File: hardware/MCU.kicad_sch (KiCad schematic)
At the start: 1 part

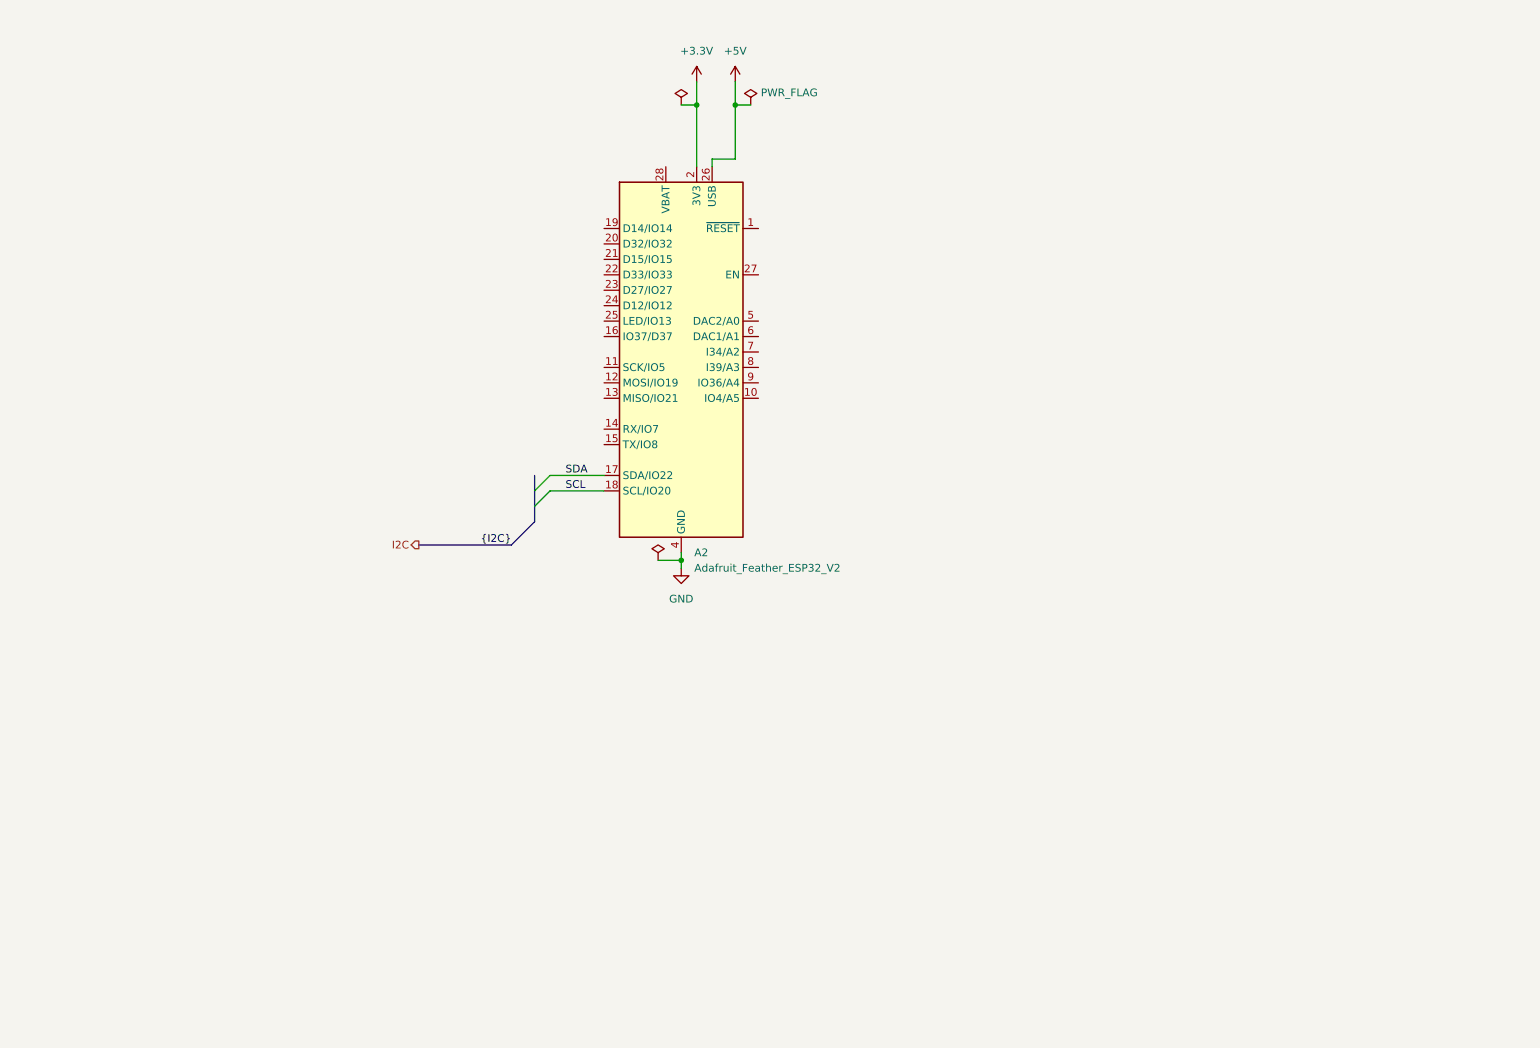
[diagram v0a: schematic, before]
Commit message: feat: Added MCP23017 SOIC GPIO Expander
Finished off the design of all of the non-GPIO pins of the expander
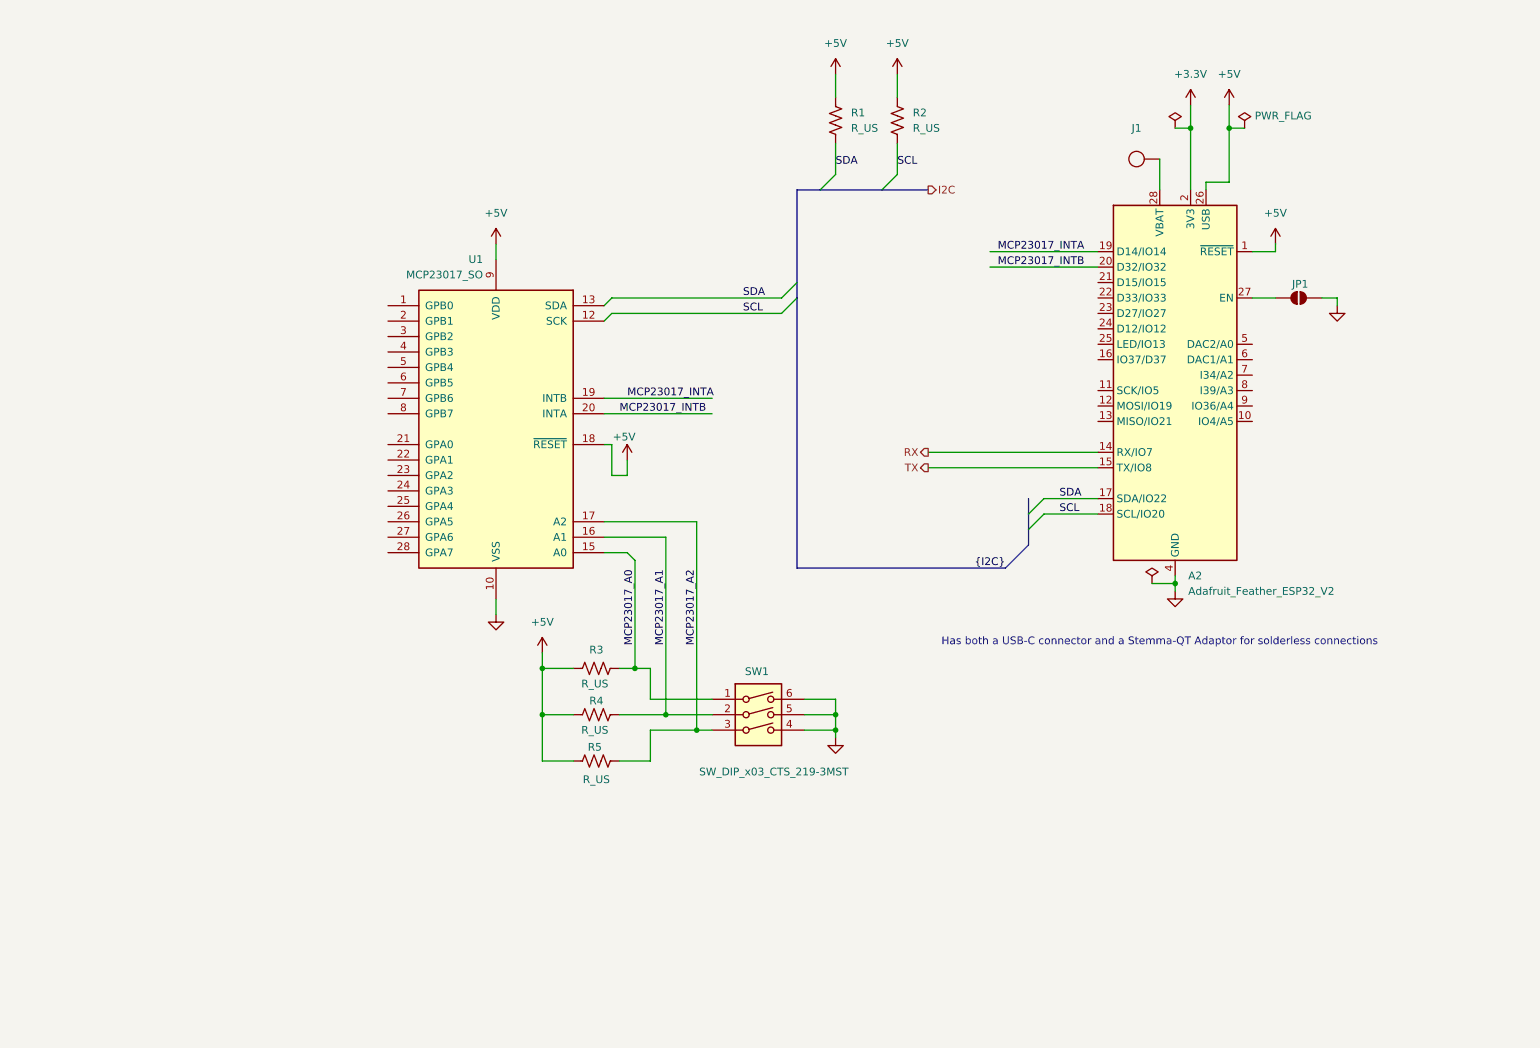
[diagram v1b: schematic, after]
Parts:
- added J1: ~, 4ms_Connector:CAPSENSE_PAD, symbol 4ms_Connector:CAPSENSE_PAD
- added JP1: SolderJumper_2_Open, Jumper:SolderJumper-2_P1.3mm_Open_Pad1.0x1.5mm, symbol Jumper:SolderJumper_2_Open
- added R1, R2, R3, R4, R5: R_US, symbol Device:R_US
- added SW1: SW_DIP_x03_CTS_219-3MST, 4ms_Switch:SW_DIP_SPSTx03_CTS_219-3MSTR, symbol 4ms_Switch:SW_DIP_x03_CTS_219-3MST
- added U1: MCP23017_SO, Package_SO:SOIC-28W_7.5x17.9mm_P1.27mm, symbol Interface_Expansion:MCP23017_SO
- A2: now left out of the parts list
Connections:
- net +5V: now also A2.1 (~{RESET}), R1.1, R2.1, R3.1, R4.1, R5.1, U1.18 (~{RESET}), U1.9 (VDD)
- net GND: now also JP1.2 (B), SW1.4, SW1.5, SW1.6, U1.10 (VSS)
- net SCL: now also R2.2, U1.12 (SCK)
- net SDA: now also R1.2, U1.13 (SDA)
- net RX: now reaches A2.14 (RX/IO7)
- net TX: now reaches A2.15 (TX/IO8)
- net MCP23017_INTA: now reaches A2.19 (D14/IO14)
- net MCP23017_INTA: now also U1.19 (INTB)
- net MCP23017_INTB: now reaches A2.20 (D32/IO32)
- net MCP23017_INTB: now also U1.20 (INTA)
- net at A2.27 (EN): now also JP1.1 (A)
- net at A2.28 (VBAT): now also J1.1 (CS)
- new net MCP23017_A0: R3.2, SW1.1, U1.15 (A0)
- new net MCP23017_A1: R4.2, SW1.2, U1.16 (A1)
- new net MCP23017_A2: R5.2, SW1.3, U1.17 (A2)
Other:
- note added: "Has both a USB-C connector and a Stemma-QT Adaptor for solderless connections"
- moved on the sheet: A2

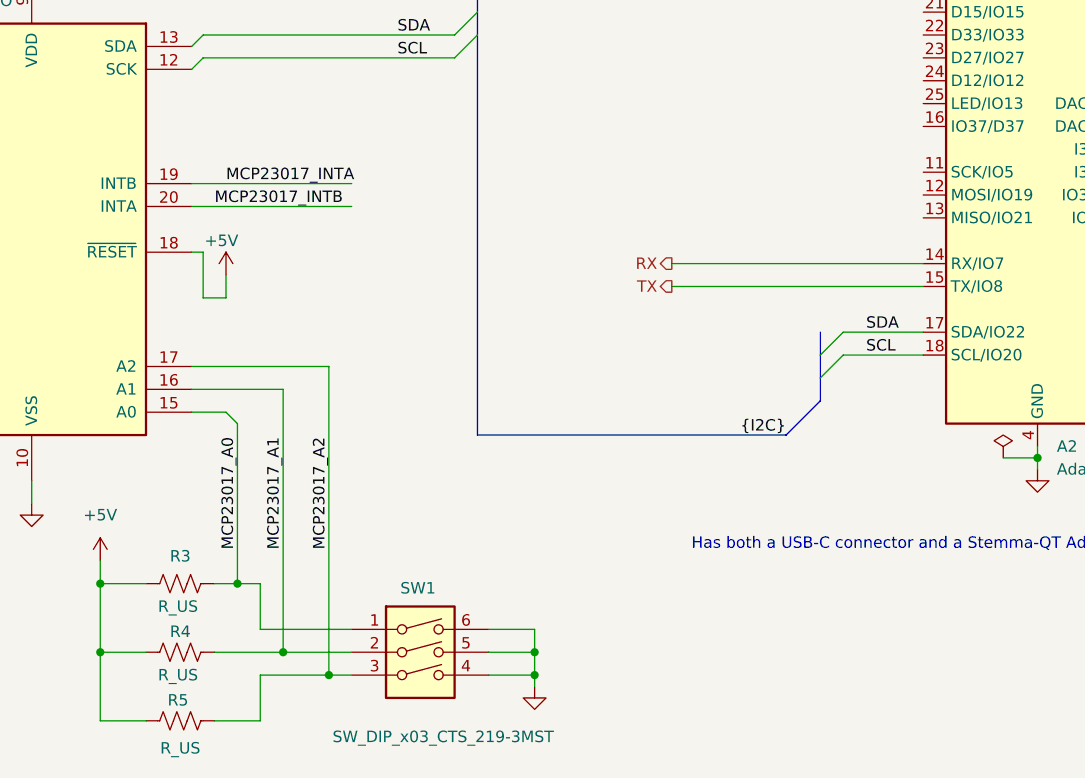
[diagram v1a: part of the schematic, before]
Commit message: feat: Created Button I2C Interfaces
For now, all we are using is generic 1x5 Connectors following the DFR Robot's RGB Button pinout https://wiki.dfrobot.com/SKU_DFR0991_Gravity_I2C_RGB_LED_Button_Module#target_9
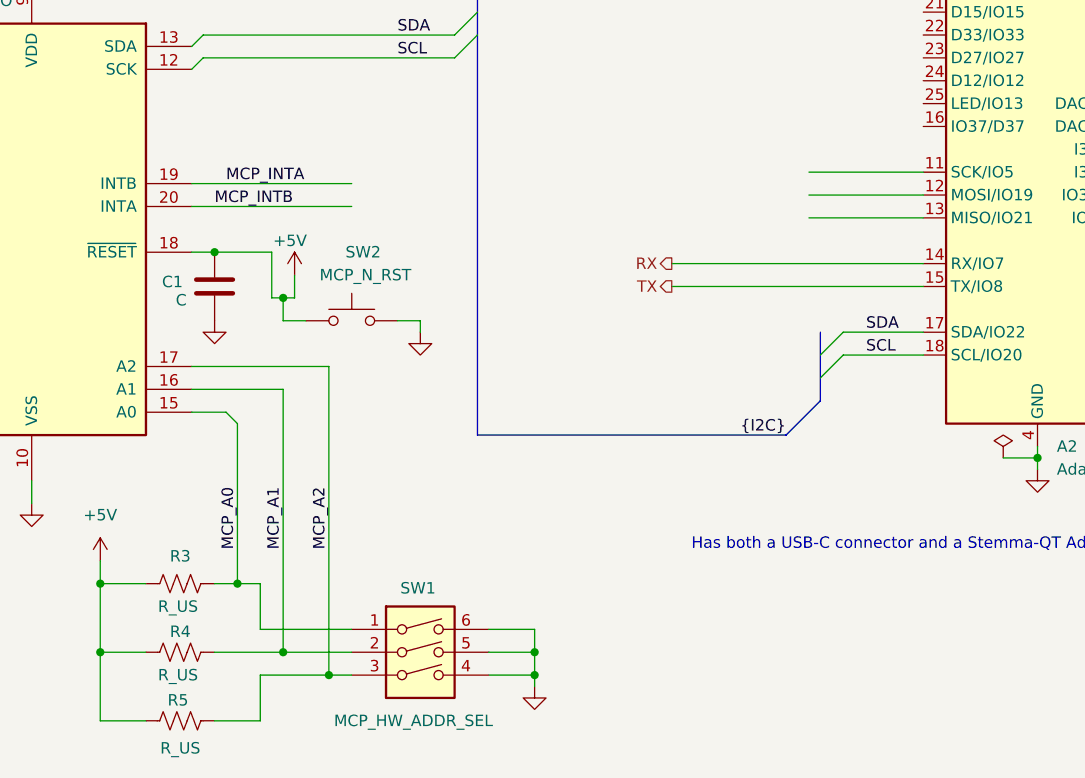
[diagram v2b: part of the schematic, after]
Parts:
- added C1: C, symbol Device:C
- added SW2: MCP_N_RST, symbol Switch:SW_Push
- SW1: value SW_DIP_x03_CTS_219-3MST -> MCP_HW_ADDR_SEL
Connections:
- net +5V: now also C1.1, SW2.1
- net GND: now also C1.2, SW2.2
- net MCP23017_INTA: no longer U1.19 (INTB)
- net MCP23017_INTB: no longer U1.20 (INTA)
- net MCP23017_A0 renamed MCP_A0
- net MCP23017_A1 renamed MCP_A1
- net MCP23017_A2 renamed MCP_A2
- new net MCP_INTA: U1.19 (INTB)
- new net MCP_INTB: U1.20 (INTA)

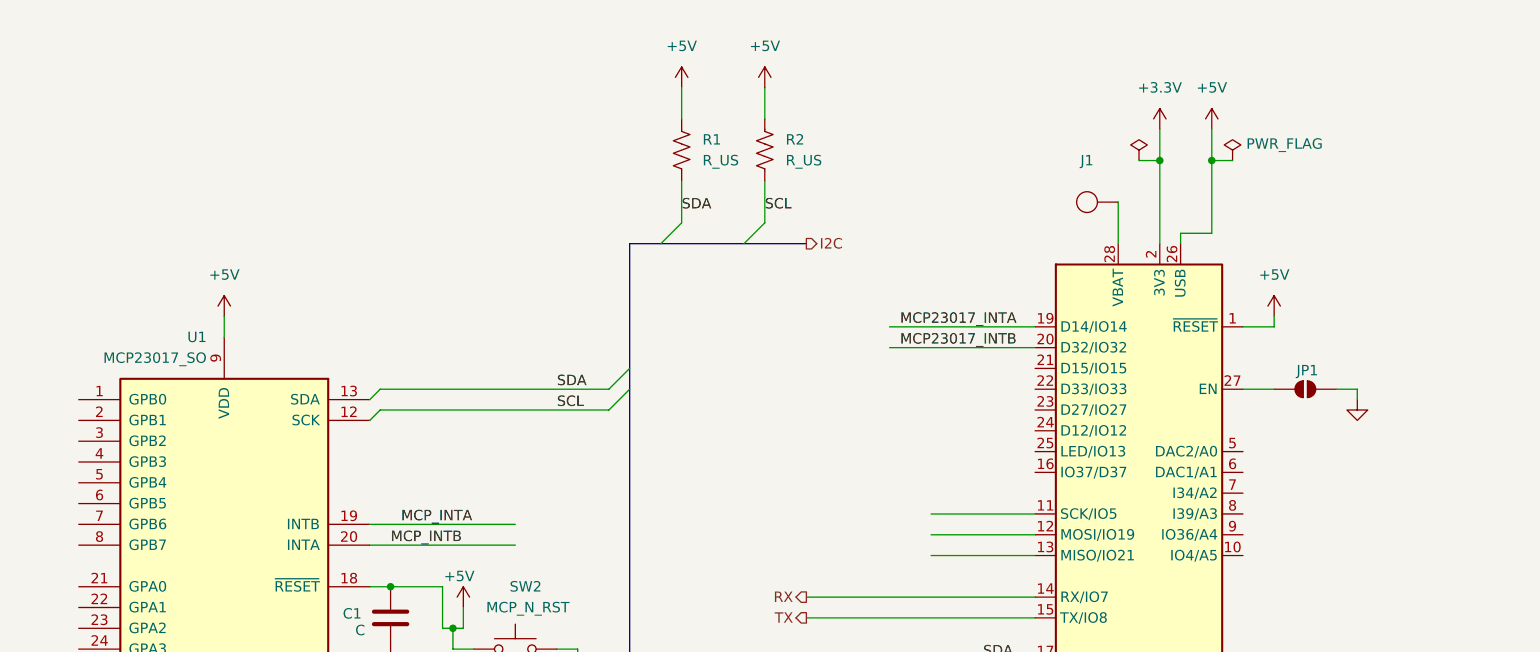
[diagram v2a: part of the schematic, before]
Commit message: feat: Added Volume and Inf Scroll Encoders
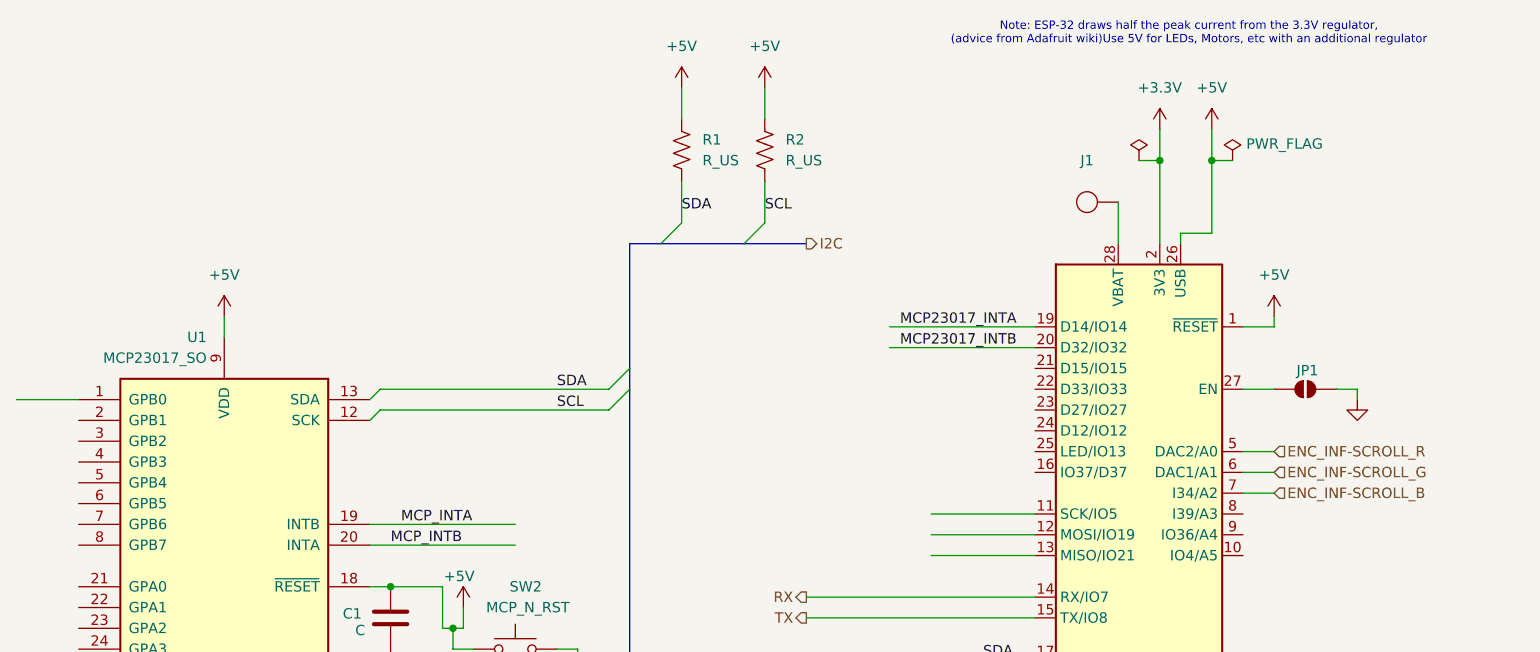
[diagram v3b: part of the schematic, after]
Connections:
- net ENC_INF-SCROLL_R: now reaches A2.5 (DAC2/A0)
- net ENC_INF-SCROLL_G: now reaches A2.6 (DAC1/A1)
- net ENC_INF-SCROLL_B: now reaches A2.7 (I34/A2)
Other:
- note added: "Note: ESP-32 draws half the peak current from the 3.3V regulator, (advice from Adafruit wiki)Use 5V for LEDs, Motors, etc with an additional regulator"
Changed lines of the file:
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@@
+		)
+	)
+	(text "Note: ESP-32 draws half the peak current from the 3.3V regulator,\n(advice from Adafruit wiki)Use 5V for LEDs, Motors, etc with an additional regulator"
+		(exclude_from_sim no)
+		(at 211.836 17.526 0)
+		(effects
+			(font
+				(size 1.016 1.016)
+			)
+			(href "https://learn.adafruit.com/adafruit-esp32-feather-v2/power-management-2")
 		)
 	)
@@
 	(wire
 		(pts
+			(xy 218.44 71.12) (xy 222.25 71.12)
+		)
+		(stroke
+			(width 0)
+			(type default)
+		)
+	)
+	(wire
+		(pts
+			(xy 218.44 68.58) (xy 222.25 68.58)
+		)
+		(stroke
+			(width 0)
+			(type default)
+		)
+	)
+	(wire
+		(pts
 			(xy 232.41 60.96) (xy 232.41 62.23)
 		)
@@
 	(wire
 		(pts
+			(xy 68.58 62.23) (xy 76.2 62.23)
+		)
+		(stroke
+			(width 0)
+			(type default)
+		)
+	)
+	(wire
+		(pts
 			(xy 93.98 110.49) (xy 93.98 113.03)
 		)
@@
 		(pts
 			(xy 119.38 127) (xy 129.54 127)
+		)
+		(stroke
+			(width 0)
+			(type default)
+		)
+	)
+	(wire
+		(pts
+			(xy 218.44 73.66) (xy 222.25 73.66)
 		)
 		(stroke
@@
 			)
 			(justify left bottom)
+		)
+	)
+	(hierarchical_label "ENC_INF-SCROLL_B"
+		(shape input)
+		(at 222.25 73.66 0)
+		(effects
+			(font
+				(size 1.27 1.27)
+			)
+			(justify left)
+		)
+	)
+	(hierarchical_label "ENC_INF-SCROLL_G"
+		(shape input)
+		(at 222.25 71.12 0)
+		(effects
+			(font
+				(size 1.27 1.27)
+			)
+			(justify left)
 		)
 	)
@@
 		)
 	)
+	(hierarchical_label "ENC_INF-SCROLL_R"
+		(shape input)
+		(at 222.25 68.58 0)
+		(effects
+			(font
+				(size 1.27 1.27)
+			)
+			(justify left)
+		)
+	)

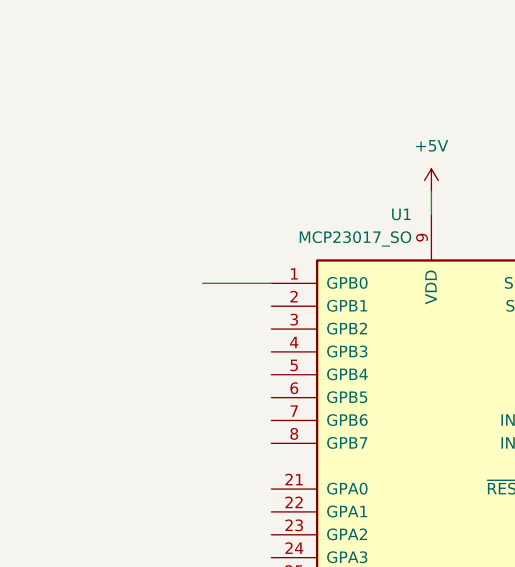
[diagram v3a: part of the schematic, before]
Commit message: feat: Added Footswitch Jack Conn for Tap Tempo
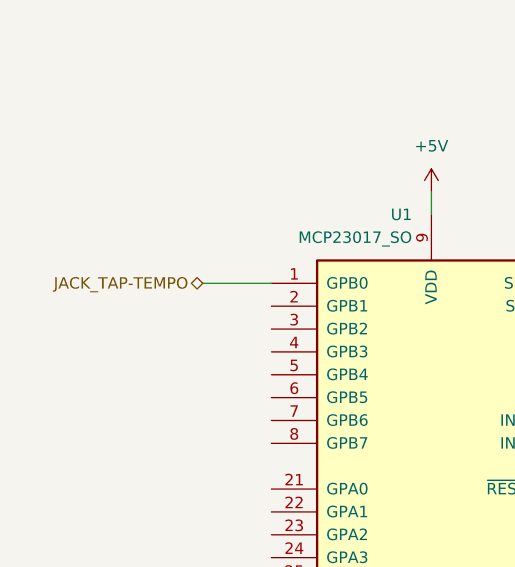
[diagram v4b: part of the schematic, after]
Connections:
- net JACK_TAP-TEMPO: now reaches U1.1 (GPB0)
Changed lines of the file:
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@@
+		)
+	)
+	(hierarchical_label "JACK_TAP-TEMPO"
+		(shape bidirectional)
+		(at 68.58 62.23 180)
+		(effects
+			(font
+				(size 1.27 1.27)
+			)
+			(justify right)
 		)
 	)
